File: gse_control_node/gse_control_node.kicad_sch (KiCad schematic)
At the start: 8 parts, among them J1 Screw_Terminal_01x02

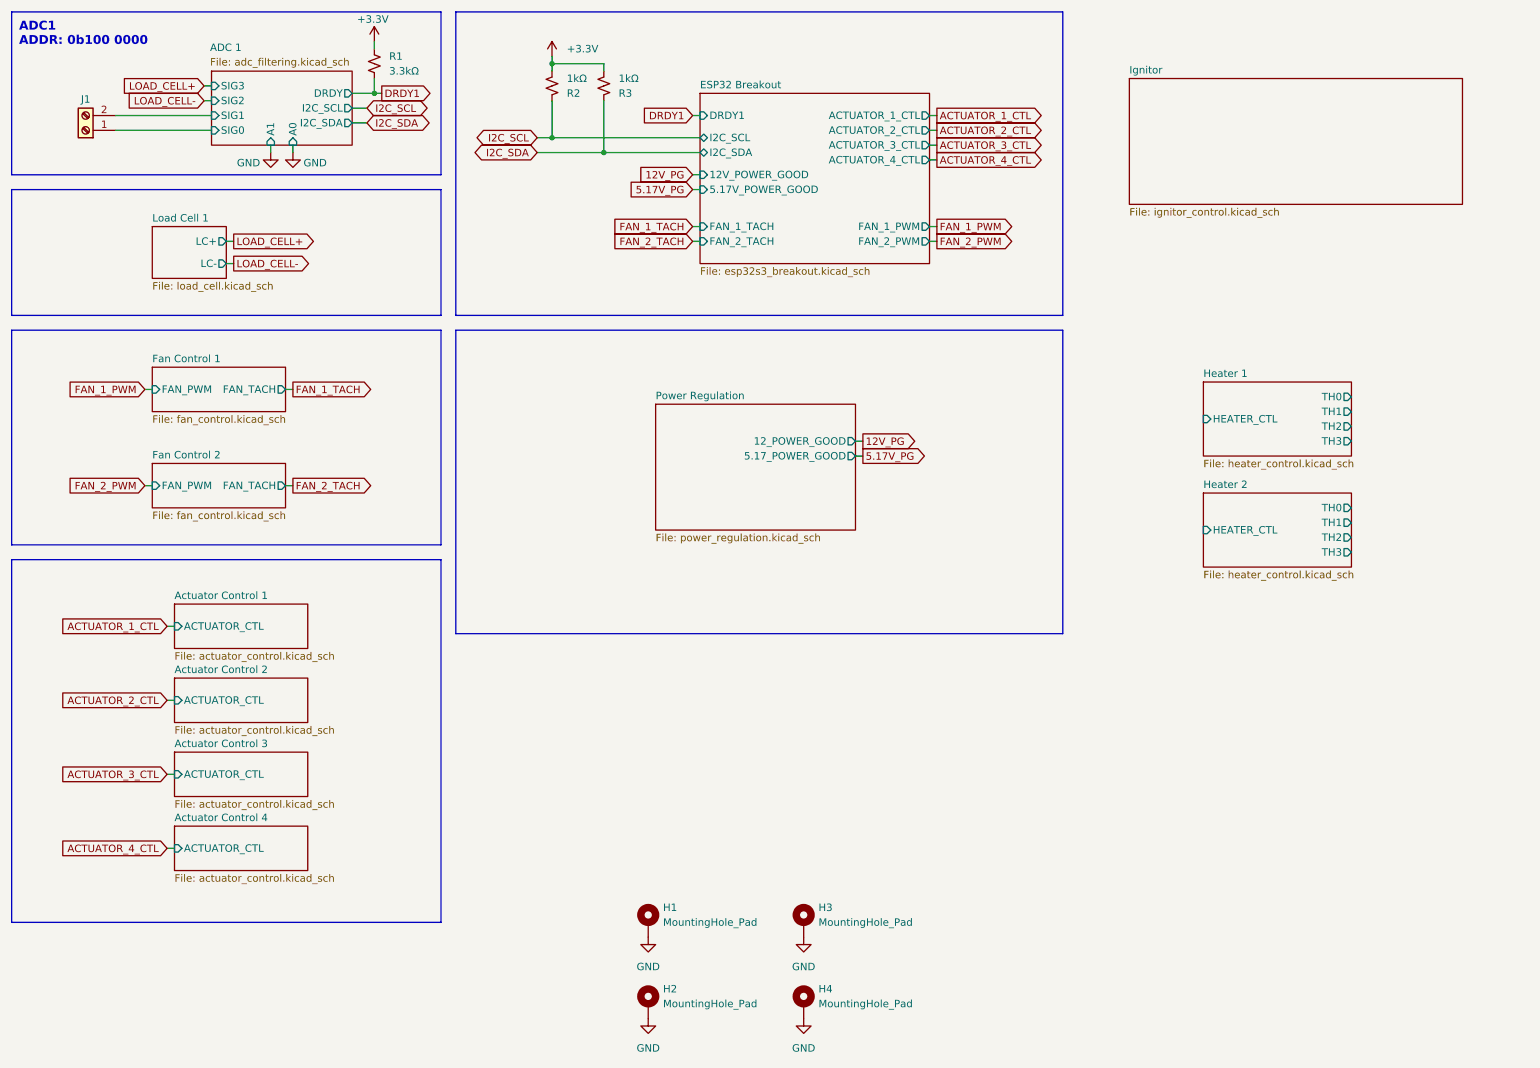
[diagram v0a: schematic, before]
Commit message: finish control board routing
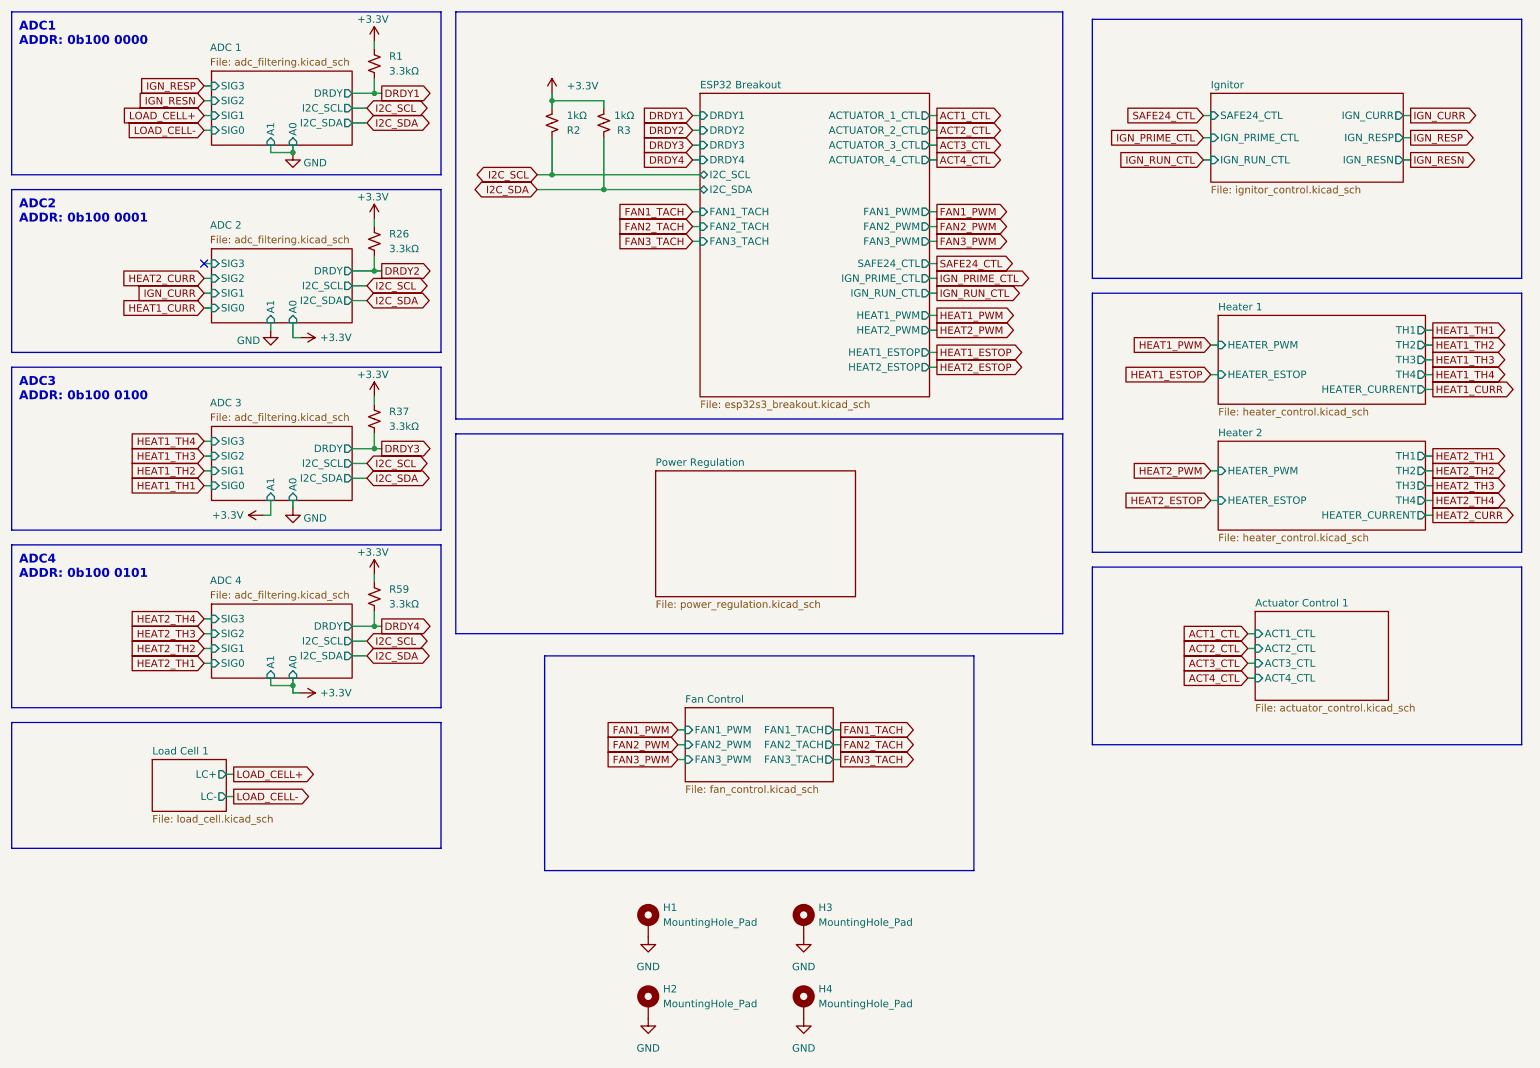
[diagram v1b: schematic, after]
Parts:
- removed J1: Screw_Terminal_01x02, TerminalBlock_CUI:TerminalBlock_CUI_TB007-508-02_1x02_P5.08mm_Horizontal, symbol Connector:Screw_Terminal_01x02
- added R26, R37, R59: 3.3kΩ, Resistor_SMD:R_0603_1608Metric, symbol Device:R_Small_US
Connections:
- net +3.3V: now also R26.1, R37.1, R59.1
- new net DRDY2: R26.2
- new net DRDY3: R37.2
- new net DRDY4: R59.2
- no-connect marks 0 -> 1
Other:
- sheet Fan Control 1 renamed Fan Control
- removed sheet Actuator Control 2
- removed sheet Actuator Control 3
- removed sheet Actuator Control 4
- removed sheet Fan Control 2
- added sheet ADC 2 (adc_filtering.kicad_sch)
- added sheet ADC 3 (adc_filtering.kicad_sch)
- added sheet ADC 4 (adc_filtering.kicad_sch)
- sheet Actuator Control 1 ports: added ACT1_CTL, ACT2_CTL, ACT3_CTL, ACT4_CTL; removed ACTUATOR_CTL
- sheet ESP32 Breakout ports: added DRDY2, DRDY3, DRDY4, FAN1_PWM, FAN1_TACH, FAN2_PWM, FAN2_TACH, FAN3_PWM, FAN3_TACH, HEAT1_ESTOP, HEAT1_PWM, HEAT2_ESTOP, HEAT2_PWM, IGN_PRIME_CTL, IGN_RUN_CTL, SAFE24_CTL; removed 12V_POWER_GOOD, 5.17V_POWER_GOOD, FAN_1_PWM, FAN_1_TACH, FAN_2_PWM, FAN_2_TACH
- sheet Fan Control ports: added FAN1_PWM, FAN1_TACH, FAN2_PWM, FAN2_TACH, FAN3_PWM, FAN3_TACH; removed FAN_PWM, FAN_TACH
- sheet Heater 1 ports: added HEATER_CURRENT, HEATER_ESTOP, HEATER_PWM, TH4; removed HEATER_CTL, TH0
- sheet Heater 2 ports: added HEATER_CURRENT, HEATER_ESTOP, HEATER_PWM, TH4; removed HEATER_CTL, TH0
- sheet Ignitor ports: added IGN_CURR, IGN_PRIME_CTL, IGN_RESN, IGN_RESP, IGN_RUN_CTL, SAFE24_CTL; removed none
- sheet Power Regulation ports: added none; removed 12_POWER_GOOD, 5.17_POWER_GOOD
- note added: "ADC2 ADDR: 0b100 0001"
- note added: "ADC3 ADDR: 0b100 0100"
- note added: "ADC4 ADDR: 0b100 0101"
- moved on the sheet: R2, R3

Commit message: updates for manufacturing
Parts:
- R1, R26, R37, R59: value 3.3kΩ -> 3.3k
- R2, R3: value 1kΩ -> 1k
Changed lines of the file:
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@@
 			)
 		)
-		(property "Value" "3.3kΩ"
+		(property "Value" "3.3k"
 			(at 80.01 55.8799 0)
 			(show_name no)
@@
 			)
 		)
-		(property "Value" "1kΩ"
+		(property "Value" "1k"
 			(at 110.49 33.0201 0)
 			(show_name no)
@@
 			)
 		)
-		(property "Value" "3.3kΩ"
+		(property "Value" "3.3k"
 			(at 80.01 86.3599 0)
 			(show_name no)
@@
 			)
 		)
-		(property "Value" "3.3kΩ"
+		(property "Value" "3.3k"
 			(at 80.01 25.3999 0)
 			(show_name no)
@@
 			)
 		)
-		(property "Value" "1kΩ"
+		(property "Value" "1k"
 			(at 118.618 33.02 0)
 			(show_name no)
@@
 			)
 		)
-		(property "Value" "3.3kΩ"
+		(property "Value" "3.3k"
 			(at 80.01 116.8399 0)
 			(show_name no)
